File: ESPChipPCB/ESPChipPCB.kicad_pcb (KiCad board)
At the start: 2 copper layers, 29 parts, among them J1 Conn_01x02, J2 Conn_01x02, J3 Conn_01x02, Q1 BPW40, Q2 BPW40, U1 ESP32-C3-WROOM-02

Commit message: More pcb stuff
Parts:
- added J4: Conn_01x02, Connector_PinHeader_2.54mm:PinHeader_1x02_P2.54mm_Vertical, F.Cu at (54.2, 101.7)
- added J6: Conn_01x02, Connector_PinHeader_2.54mm:PinHeader_1x02_P2.54mm_Vertical, F.Cu at (51.6, 98.1)
- added R10: R, Resistor_SMD:R_0603_1608Metric, F.Cu at (78.4, 129.8)
- D2, D3: footprint LED_SMD:LED-APA102-2020 -> LED_THT:LED_D5.0mm_Clear
- R8, R9: value 10K -> 10k
- moved C1 117.8 mm to (53.2, 149.6), turned to 180 degrees
- moved R7 116.4 mm to (59.2, 152.7), turned to 180 degrees
- moved C2 113.8 mm to (53.2, 148.0), turned to 180 degrees
- moved R1 111.1 mm to (53.2, 146.5)
- moved R2 110.2 mm to (50.9, 147.4), turned to 90 degrees
- moved C4 107.6 mm to (57.2, 147.7), turned to 180 degrees
- moved C5 106.7 mm to (57.2, 149.2), turned to 180 degrees
- moved C3 102.7 mm to (55.2, 139.6), turned to -90 degrees
- moved R5 98.0 mm to (78.4, 132.8), turned to 90 degrees
- moved C7 97.4 mm to (47.6, 124.8), turned to -90 degrees
- moved D3 97.3 mm to (75.2, 150.2), turned to -90 degrees
- moved R4 96.4 mm to (61.2, 141.1), turned to -90 degrees
- moved R3 94.9 mm to (62.0, 137.3), turned to 180 degrees
- moved C8 94.5 mm to (49.1, 124.8), turned to -90 degrees
- moved C6 93.0 mm to (62.0, 138.8), turned to 180 degrees
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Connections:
- D3 pad 1: Net-(D2-A) -> GND
- R8 pad 1: +3.3V -> Net-(U1-IO8)
- R8 pad 2: Net-(U1-IO2) -> +3.3V
- R9 pad 1: +3.3V -> Net-(U1-IO2)
- R9 pad 2: Net-(U1-IO8) -> +3.3V
- U1 pad 15: unconnected-(U1-IO3-Pad15) -> /FirstSensor
- U1 pad 4: unconnected-(U1-IO5-Pad4) -> /SecondSensor
- U1 pad 8: unconnected-(U1-IO9-Pad8) -> Net-(U1-IO9)
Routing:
- net +3.3V: track 0.00 -> 102.7 mm, vias 0 -> 2
- net Net-(D2-A): track 0.00 -> 49.8 mm
- net /SecondSensor: track 0.00 -> 48.6 mm
- net /FirstSensor: track 0.00 -> 38.4 mm
- net Net-(D3-A): track 0.00 -> 21.5 mm
- net /V_FB: track 0.00 -> 18.6 mm
- net +BATT: track 0.00 -> 12.4 mm
- net GND: track 0.00 -> 11.4 mm, vias 0 -> 8
- net Net-(D1-K): track 0.00 -> 8.15 mm
- net Net-(S1-NO): track 0.00 -> 6.52 mm
- net Net-(PS1-EN): track 0.00 -> 6.01 mm
- net /D-: track 0.00 -> 3.26 mm
- net /D+: track 0.00 -> 3.19 mm
- net Net-(PS1-BST): track 0.00 -> 2.12 mm
- net Net-(U1-IO2): track 0.00 -> 1.88 mm
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- added copper zone on B.Cu, net GND
- added copper zone on F.Cu, net GND
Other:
- board outline added: 47.5 x 74 mm

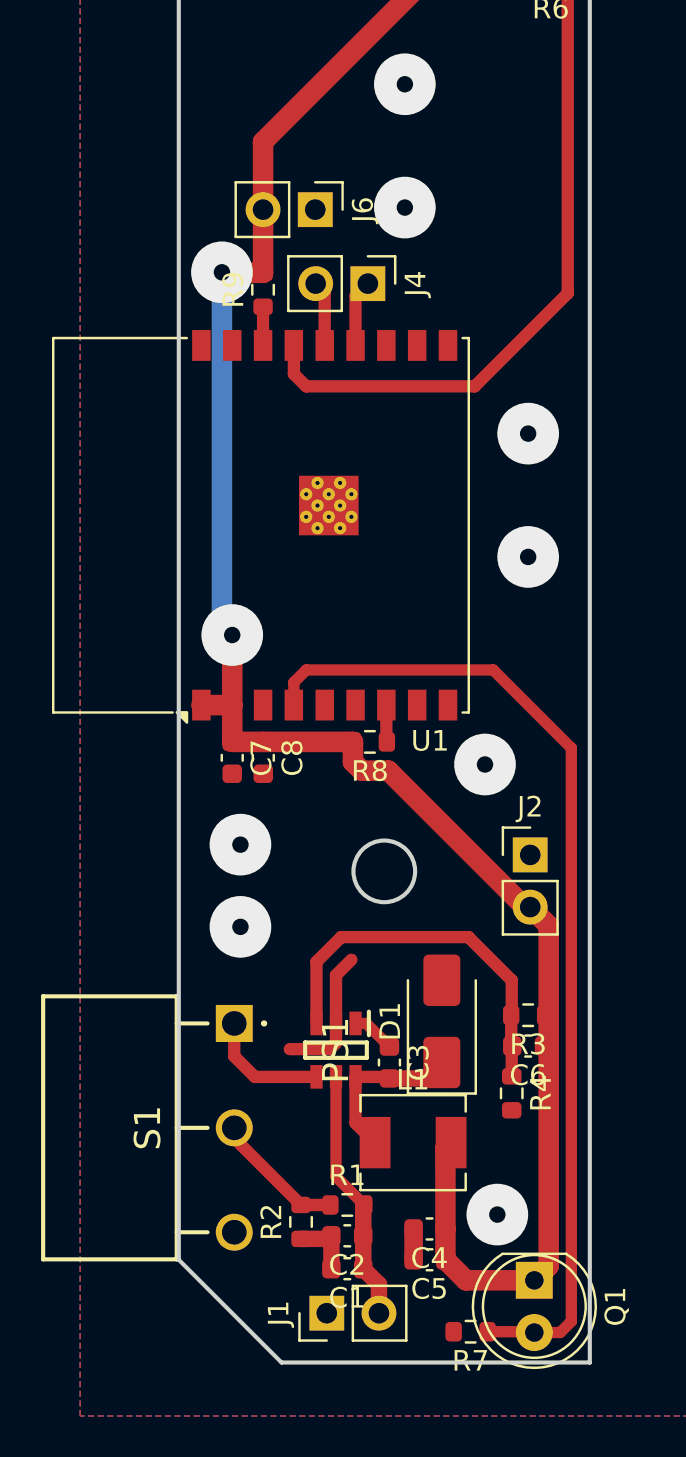
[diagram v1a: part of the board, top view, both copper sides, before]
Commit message: Moved from arduino to platformio , redone some of the code
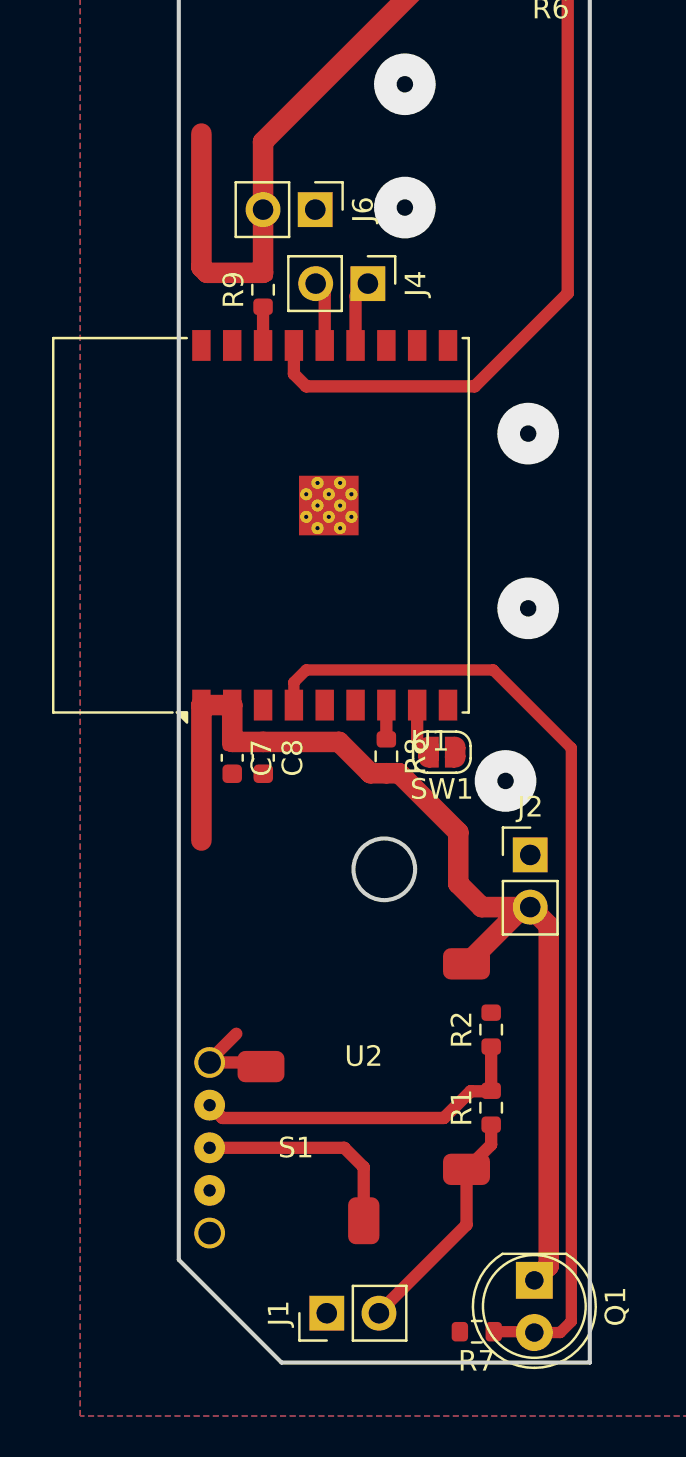
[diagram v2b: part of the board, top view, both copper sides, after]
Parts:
- removed C1, C2: 10u/1206, Capacitor_SMD:C_0603_1608Metric
- removed C3: 22n, Capacitor_SMD:C_0603_1608Metric
- removed C4, C5: 22u, Capacitor_SMD:C_0603_1608Metric
- removed C6: 100p, Capacitor_SMD:C_0603_1608Metric
- removed D1: B340A, Diode_SMD:D_SMA
- removed L1: 10u/C2921170, Inductor_SMD:L_Chilisin_BMRA00040420
- removed PS1: AP5100WG-7, SamacSys:SOT95P285X140-6N
- removed R3: 10k, Resistor_SMD:R_0603_1608Metric
- removed R4: 3.3k, Resistor_SMD:R_0603_1608Metric
- added SW1: SW_Push, Jumper:SolderJumper-2_P1.3mm_Open_RoundedPad1.0x1.5mm, F.Cu at (57.8, 124.5)
- added U2: ~, SamacSys:StepDown3v3, F.Cu at (54.0, 139.8)
- R2: value 2k -> 10k
- S1: value EN -> Trigger; footprint SamacSys:463092691402 -> SamacSys:SwitchSmall
- moved R2 13.2 mm to (60.2, 138.0)
- moved R1 8.45 mm to (60.2, 141.8), turned to 90 degrees
- moved S1 6.17 mm to (46.5, 143.8), turned to 0 degrees
- moved R8 1.06 mm to (55.1, 124.7), turned to -90 degrees
- moved R7 0.30 mm to (59.5, 152.7)
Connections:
- R1 pad 1: Net-(S1-NO) -> +BATT
- R1 pad 2: +BATT -> Net-(S1-COM)
- R2 pad 1: GND -> Net-(S1-COM)
- R2 pad 2: Net-(S1-NO) -> GND
- S1 pad 1: Net-(PS1-EN) -> Net-(S1-COM)
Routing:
- net /V_FB: track 18.6 -> 0.00 mm
- net Net-(S1-COM): track 0.00 -> 16.7 mm
- net +3.3V: track 102.7 -> 90.2 mm, vias 2 -> 0
- net Net-(D1-K): track 8.15 -> 0.00 mm
- net GND: track 11.4 -> 4.42 mm, vias 8 -> 5
- net Net-(PS1-EN): track 6.01 -> 0.00 mm
- net Net-(S1-NO): track 6.52 -> 10.5 mm
- net Net-(U1-IO9): track 0.00 -> 2.52 mm
- net Net-(PS1-BST): track 2.12 -> 0.00 mm
- net +BATT: track 12.4 -> 11.4 mm
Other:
- outline, holes or cut-outs redrawn

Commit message: Redone logic and calculations
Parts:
- R10, R5: value R -> 200
- moved R7 18.3 mm to (63.2, 134.8), turned to 0 degrees
- moved R6 2.92 mm to (63.4, 89.8), turned to 0 degrees
- moved Q1 2.55 mm to (62.3, 152.8), turned to 90 degrees
- moved Q2 2.55 mm to (62.3, 81.7), turned to -90 degrees
- moved J6 1.90 mm to (51.6, 96.2)
- moved J4 1.70 mm to (54.2, 100.0)
- moved SW1 1.02 mm to (58.8, 124.7)
- moved R2 0.80 mm to (60.2, 138.8)
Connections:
- Q1 pad 1: +3.3V -> /SecondSensor
- Q1 pad 2: /SecondSensor -> GND
- Q2 pad 1: +3.3V -> /FirstSensor
- Q2 pad 2: /FirstSensor -> GND
- R6 pad 1: /FirstSensor -> +3.3V
- R6 pad 2: GND -> /FirstSensor
- R7 pad 1: /SecondSensor -> +3.3V
- R7 pad 2: GND -> /SecondSensor
- U1 pad 10: unconnected-(U1-IO10-Pad10) -> /FirstSensor
- U1 pad 15: /FirstSensor -> unconnected-(U1-IO3-Pad15)
- U1 pad 4: /SecondSensor -> unconnected-(U1-IO5-Pad4)
- U1 pad 6: unconnected-(U1-IO7-Pad6) -> /SecondSensor
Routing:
- net +3.3V: track 90.2 -> 72.0 mm
- net /FirstSensor: track 38.4 -> 27.2 mm
- net /SecondSensor: track 48.3 -> 46.4 mm
- net /D+: track 3.19 -> 4.89 mm
- net /D-: track 3.26 -> 4.96 mm
- net Net-(U1-IO9): track 2.52 -> 3.63 mm
- net Net-(S1-COM): track 16.7 -> 15.9 mm
- net GND: vias 5 -> 4
